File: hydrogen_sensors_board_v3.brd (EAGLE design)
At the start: 100 x 100 mm, 79 parts, among them CN1 1X4-CLEANBIG, IC1 317T, IC2 LM741D, U1 ATMEGA328P_TQFP, Y1 16MHz

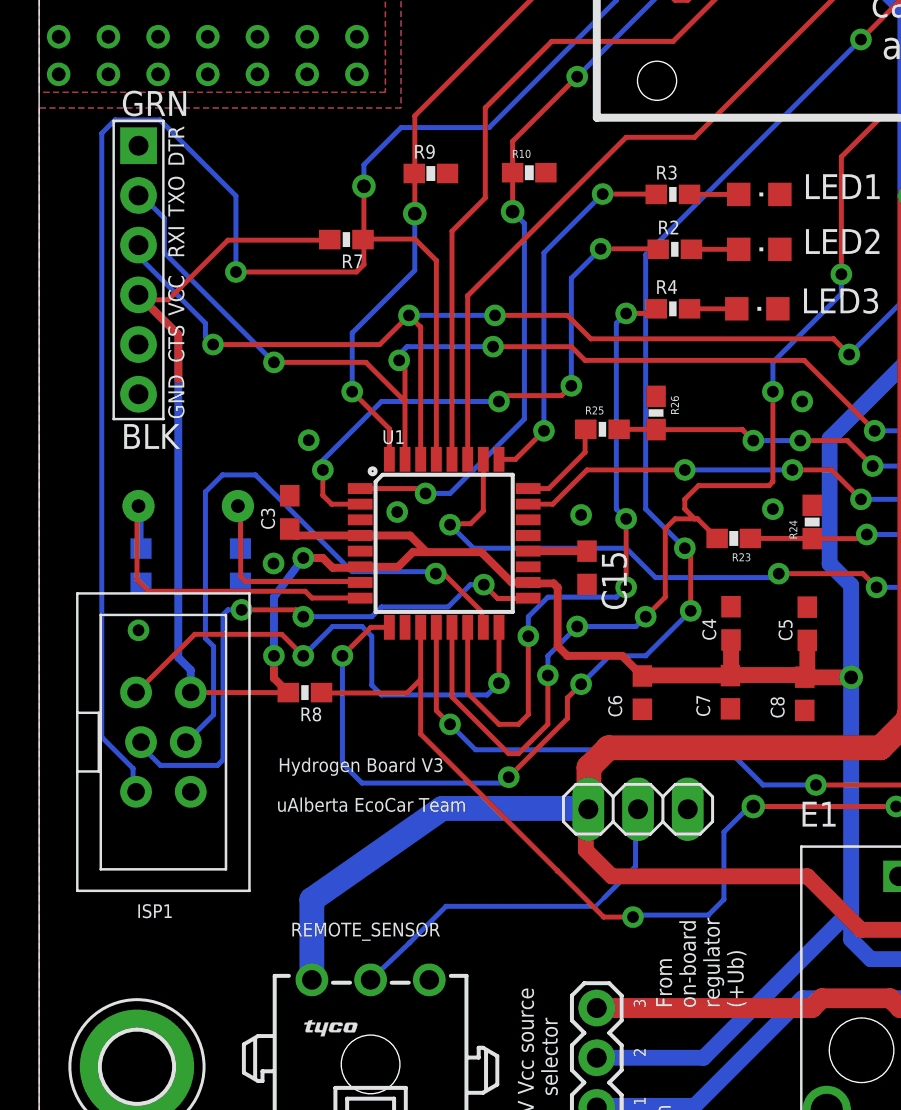
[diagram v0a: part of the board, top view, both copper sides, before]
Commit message: Added decoupling caps and inductor
100nF cap moved closer to VCC pin on right side of ATmega, added
inductor on AVCC line which then connects to 5V line. This is for more
accurate ADC measurements as noted in datasheet. 100nF cap also added to
12V line for decoupling.
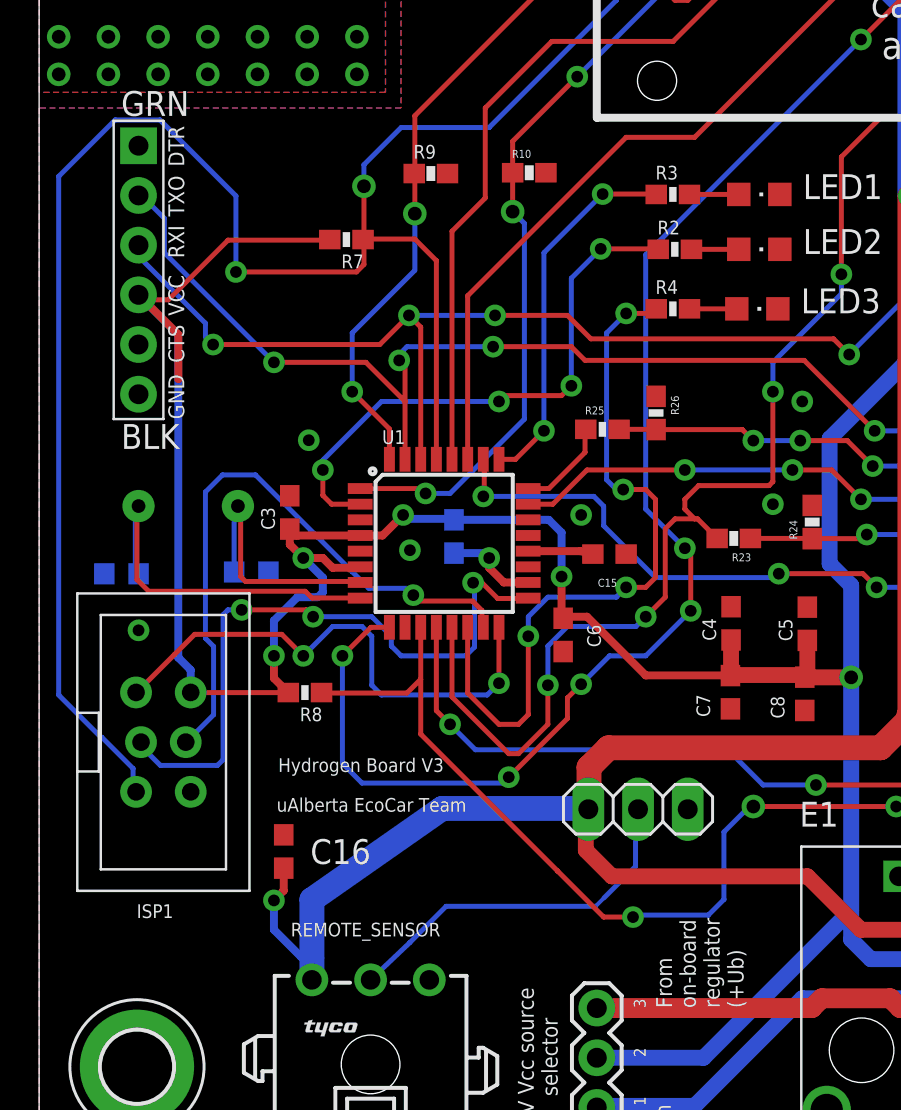
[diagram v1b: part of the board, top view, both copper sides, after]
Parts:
- added C16: 100nF, adafruit:C0603
- added L1: 100uH, SparkFun:0603
- moved C6 5.01 mm to (26.8, 27.1)
- moved C15 1.35 mm to (29.1, 31.2), turned to 0 degrees
- moved C1 1.08 mm to (4.21, 30.2), turned to 0 degrees
- moved C2 0.64 mm to (10.8, 30.3), turned to 180 degrees
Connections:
- new net N$6: L1.2, U1.18
- net +12V: now also C16.1
- net +5V: now also L1.1; no longer U1.18
- net GND: now also C16.2
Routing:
- net +12V: track 168.2 -> 174.1 mm, vias 2 -> 3
- net N$6: track 0.00 -> 4.71 mm, vias 0 -> 1
- net SCK: track 29.1 -> 33.2 mm
- net H2OUT: track 155.5 -> 152.3 mm
- net LED3_SIG: track 34.0 -> 37.1 mm
- net ATM_RESET: track 151.7 -> 153.6 mm
- net N$1: track 12.1 -> 13.5 mm
- net N$3: track 17.8 -> 19.2 mm
- net +5V: track 348.4 -> 349.2 mm, vias 10 -> 12
- net H2_OK_5V: track 111.6 -> 111.9 mm, vias 7 -> 6

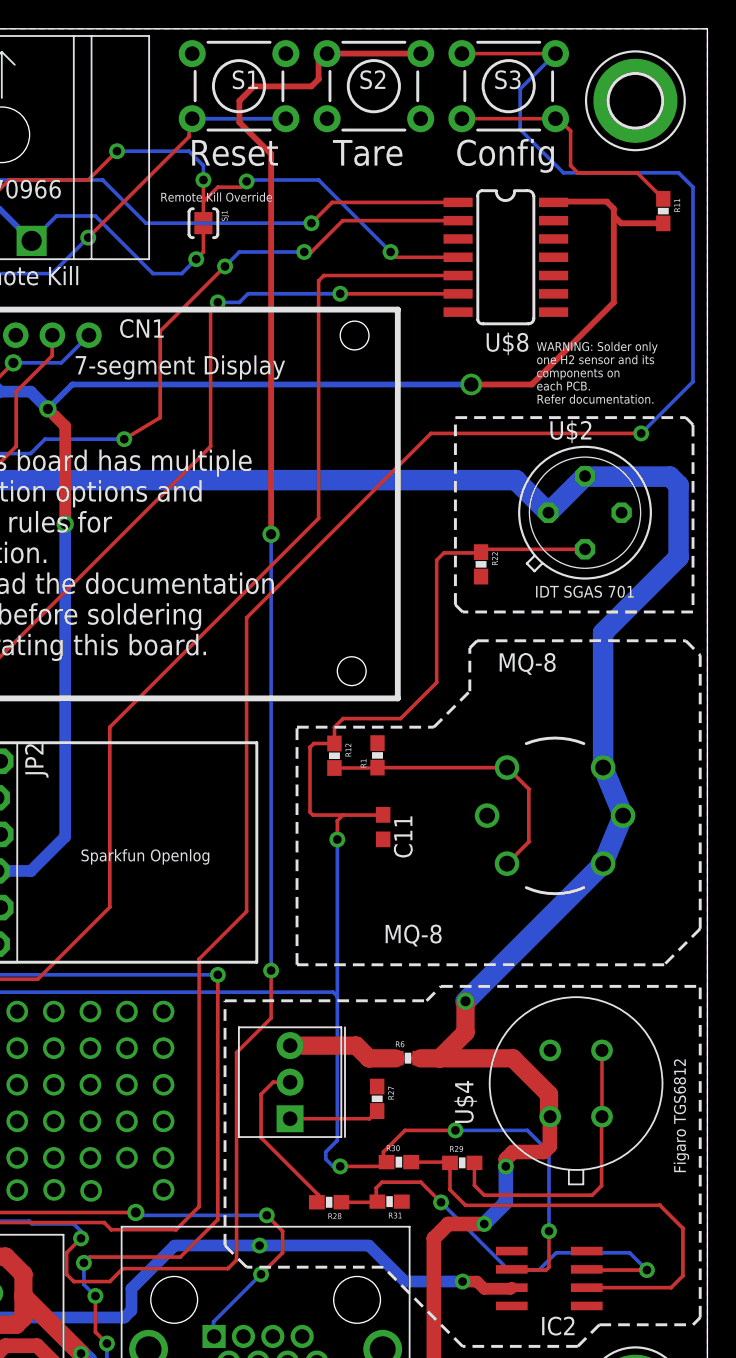
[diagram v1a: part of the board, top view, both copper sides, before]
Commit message: Noise filtering, R_s sensor voltage updated, updated README, brd and sch cleaned up
Noise filtering
Added low-pass filters to IDT SGAS and Figaro sensors.

R_s sensor voltage updated
IDT SGAS sensor's R_s voltage changed to 5V Vcc from 5.4V Regulator
output (Ub). Datasheet says max permitted voltage for R_s is 5V.

Updated README
Links to preliminary documentation and folder on Gdrive with other
files.

brd and sch cleaned up
Buttons moved a bit to the left, MQ-8 sensor schematic mirrored to match
other sensors.
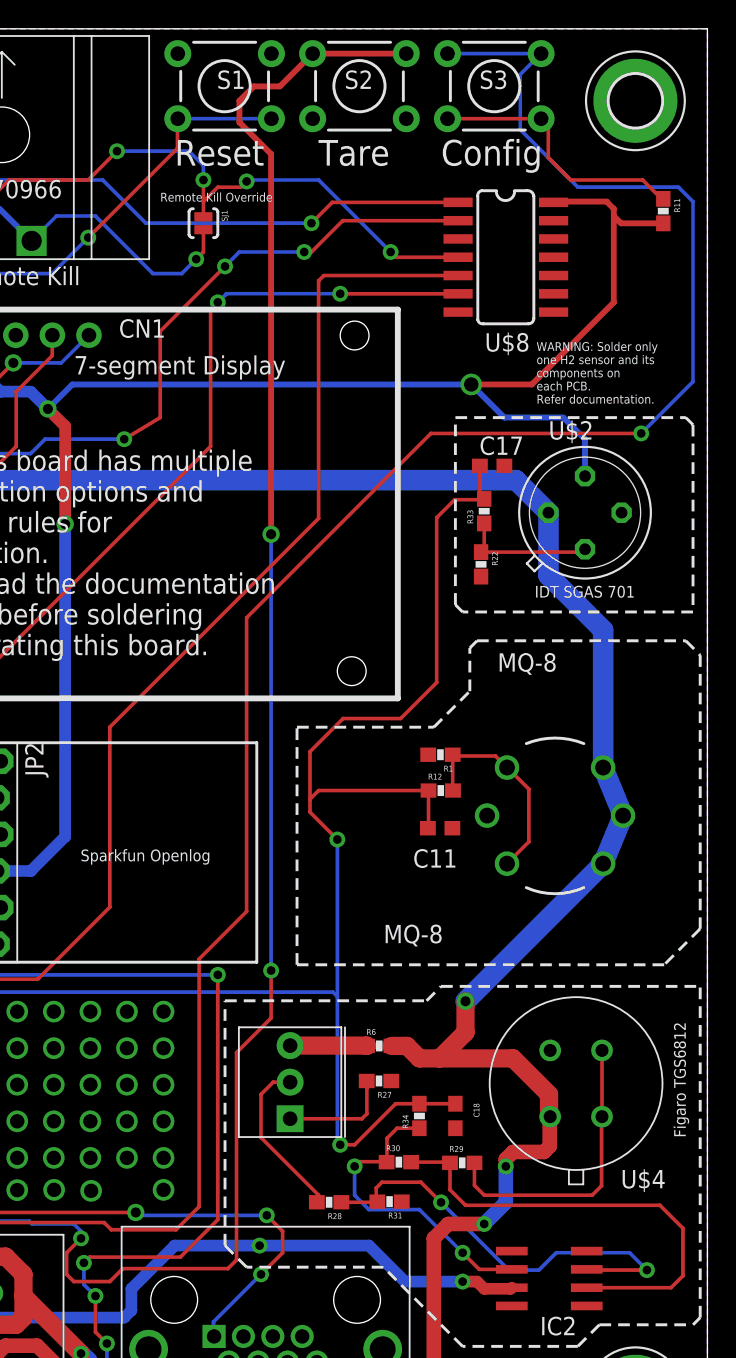
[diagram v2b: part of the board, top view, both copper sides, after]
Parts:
- added C17, C18: 100nF, adafruit:C0603
- added R33, R34: 20k, SparkFun-Passives:0603-RES
- moved R12 7.77 mm to (81.5, 47.1), turned to 0 degrees
- moved R1 4.37 mm to (81.5, 49.6), turned to 180 degrees
- moved C11 3.96 mm to (81.4, 44.5), turned to 0 degrees
- moved R6 2.17 mm to (77.2, 29.4)
- moved R27 1.25 mm to (77.2, 26.9), turned to 180 degrees
- moved S1 1.00 mm to (66.5, 96.0)
- moved S2 1.00 mm to (75.8, 96.0)
- moved S3 1.00 mm to (85.2, 96.0)
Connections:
- new net N$20: IC2.6, R30.1, R34.1
- new net N$5: R22.1, R33.1, U$2.4
- net +5V: now also U$2.2
- net +UB: no longer U$2.2
- net GND: now also C17.2, C18.2
- net H2OUT: now also C17.1, C18.1, R33.2, R34.2; no longer IC2.6, R22.1, R30.1, U$2.4
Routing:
- net N$20: track 0.00 -> 21.6 mm, vias 0 -> 2
- net H2OUT: track 152.3 -> 135.8 mm, vias 7 -> 5
- net +5V: track 349.2 -> 361.3 mm
- net +UB: track 251.3 -> 240.8 mm
- net N$5: track 0.00 -> 9.39 mm
- net N$18: track 19.9 -> 14.6 mm
- net N$2: track 7.71 -> 5.35 mm
- net TARE: track 169.9 -> 168.2 mm
- net N$10: track 6.27 -> 7.75 mm
- net N$15: track 172.1 -> 171.1 mm
- net N$16: track 17.7 -> 18.6 mm

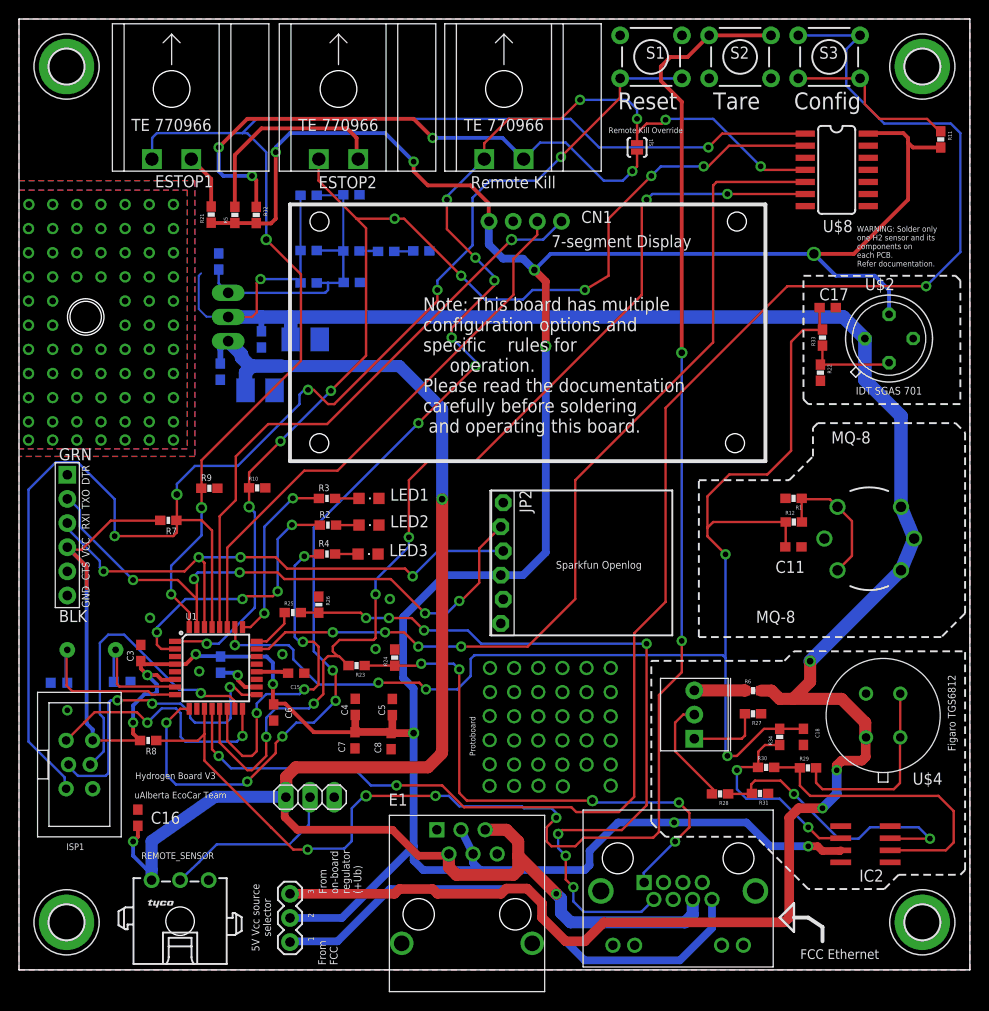
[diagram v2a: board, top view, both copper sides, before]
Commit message: Inductor value, multimeter probe points, README
Inductor value
Changed inductor value on MCU AVCC pin to 10uH per datasheet
recommendation.

Multimeter probe points
Added two probe points for the two arms of the Wheatstone bridge for the
Figaro H2 sensor circuit. Will make it easy to measure voltage between
the two arms when adjusting the potentiometer in clean air.

README
Updated links and heading in README.
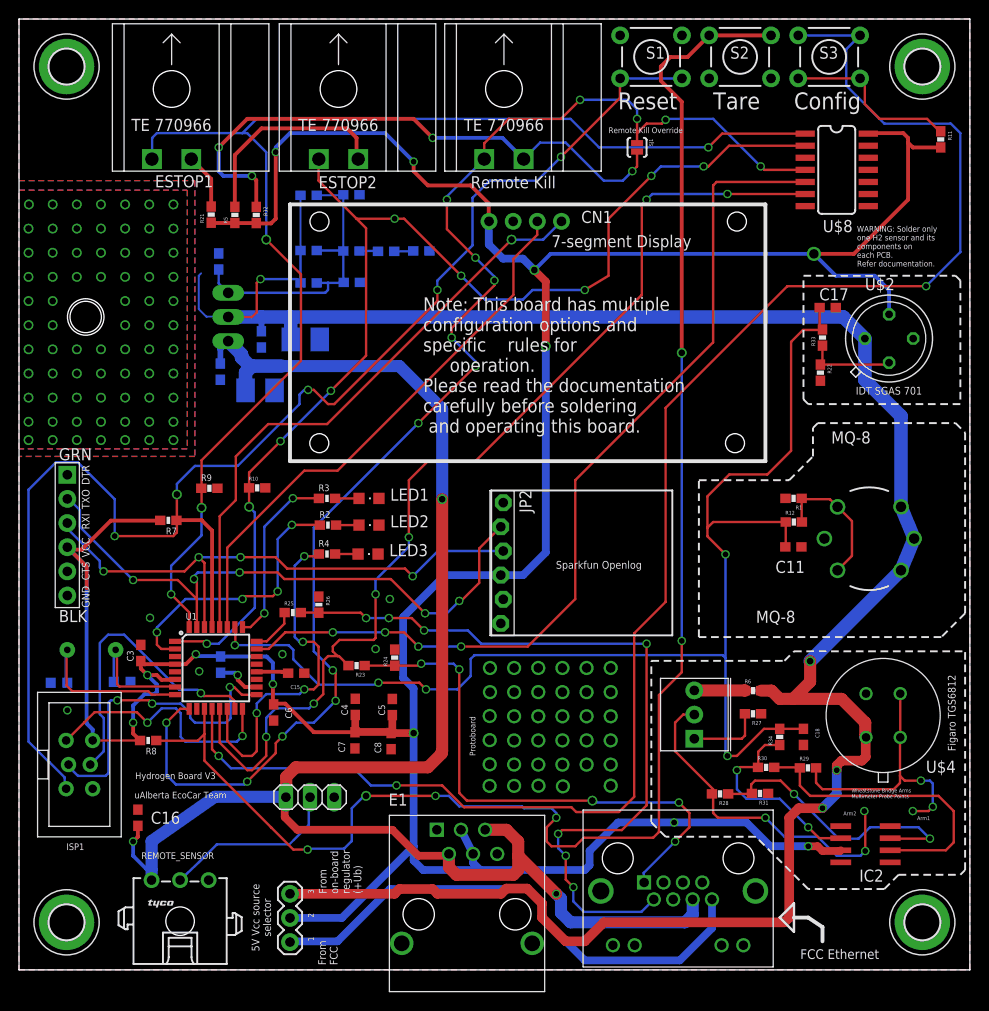
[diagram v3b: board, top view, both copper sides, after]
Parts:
- L1: value 100uH -> 10uH
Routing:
- net WB_ARM2: track 11.6 -> 36.1 mm, vias 0 -> 3
- net WB_ARM1: track 20.4 -> 28.9 mm, vias 0 -> 3
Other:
- board text added: "Arm1"
- board text added: "Arm2"
- board text added: "Wheatstone Bridge Arms Multimeter Probe Points"

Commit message: Added more decoupling caps
Added 100uF electrolytic, through-hole caps to regulator input and output. These caps are in addition to the ceramic and tantalum caps already present. Also added one more 100nF cap near the MCU.
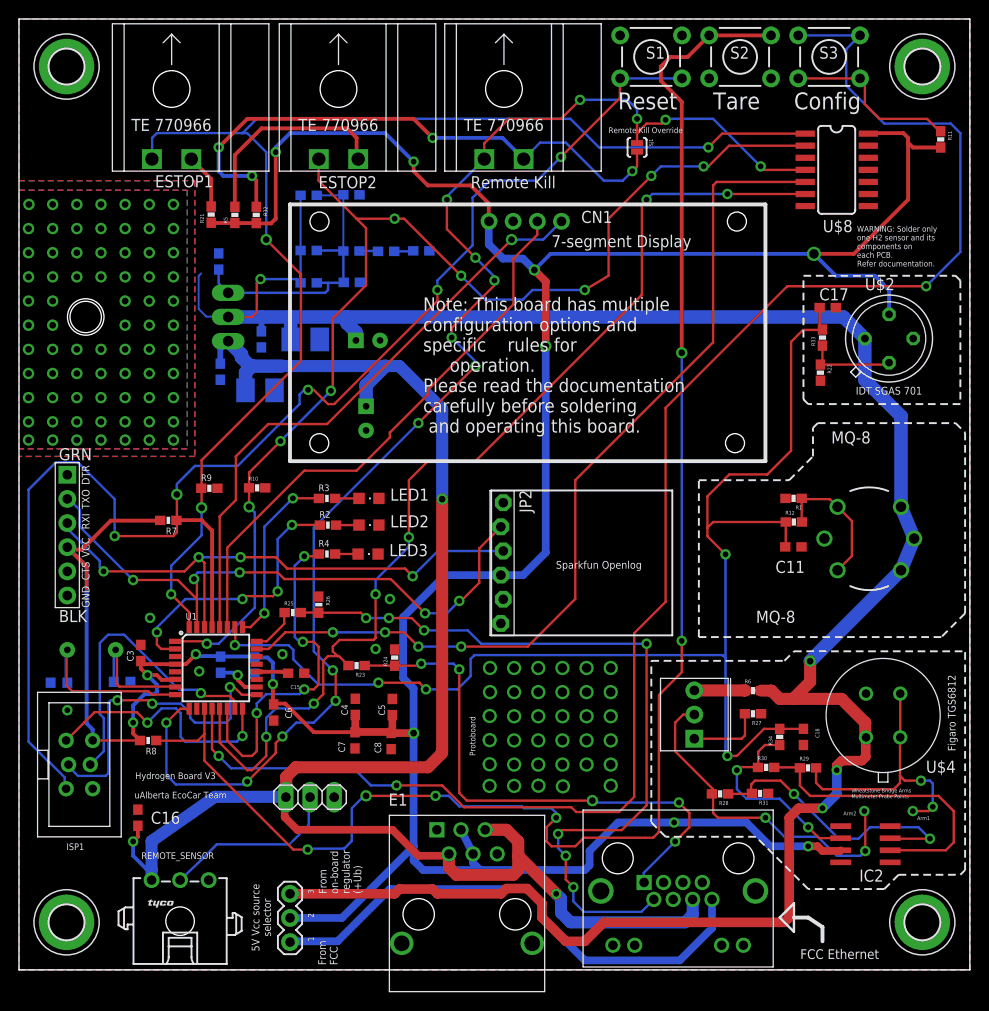
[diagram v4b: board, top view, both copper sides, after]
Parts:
- added C19, C20: 100uF, SparkFun-Capacitors:CPOL-RADIAL-100UF-25V
- added C21: 100nF, adafruit:C0603
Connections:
- net +12V: now also C20.1
- net +5V: now also C21.1
- net +UB: now also C19.1
- net GND: now also C19.2, C20.2, C21.2
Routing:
- net +12V: track 174.1 -> 179.1 mm
- net +UB: track 240.8 -> 243.7 mm
- net SDA: track 58.2 -> 59.4 mm
